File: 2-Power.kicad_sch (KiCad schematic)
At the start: 17 parts, among them J201 DC IN 5.5/2.1mm, J202 9V battery clip, U201 ZXMP3A17E6TA

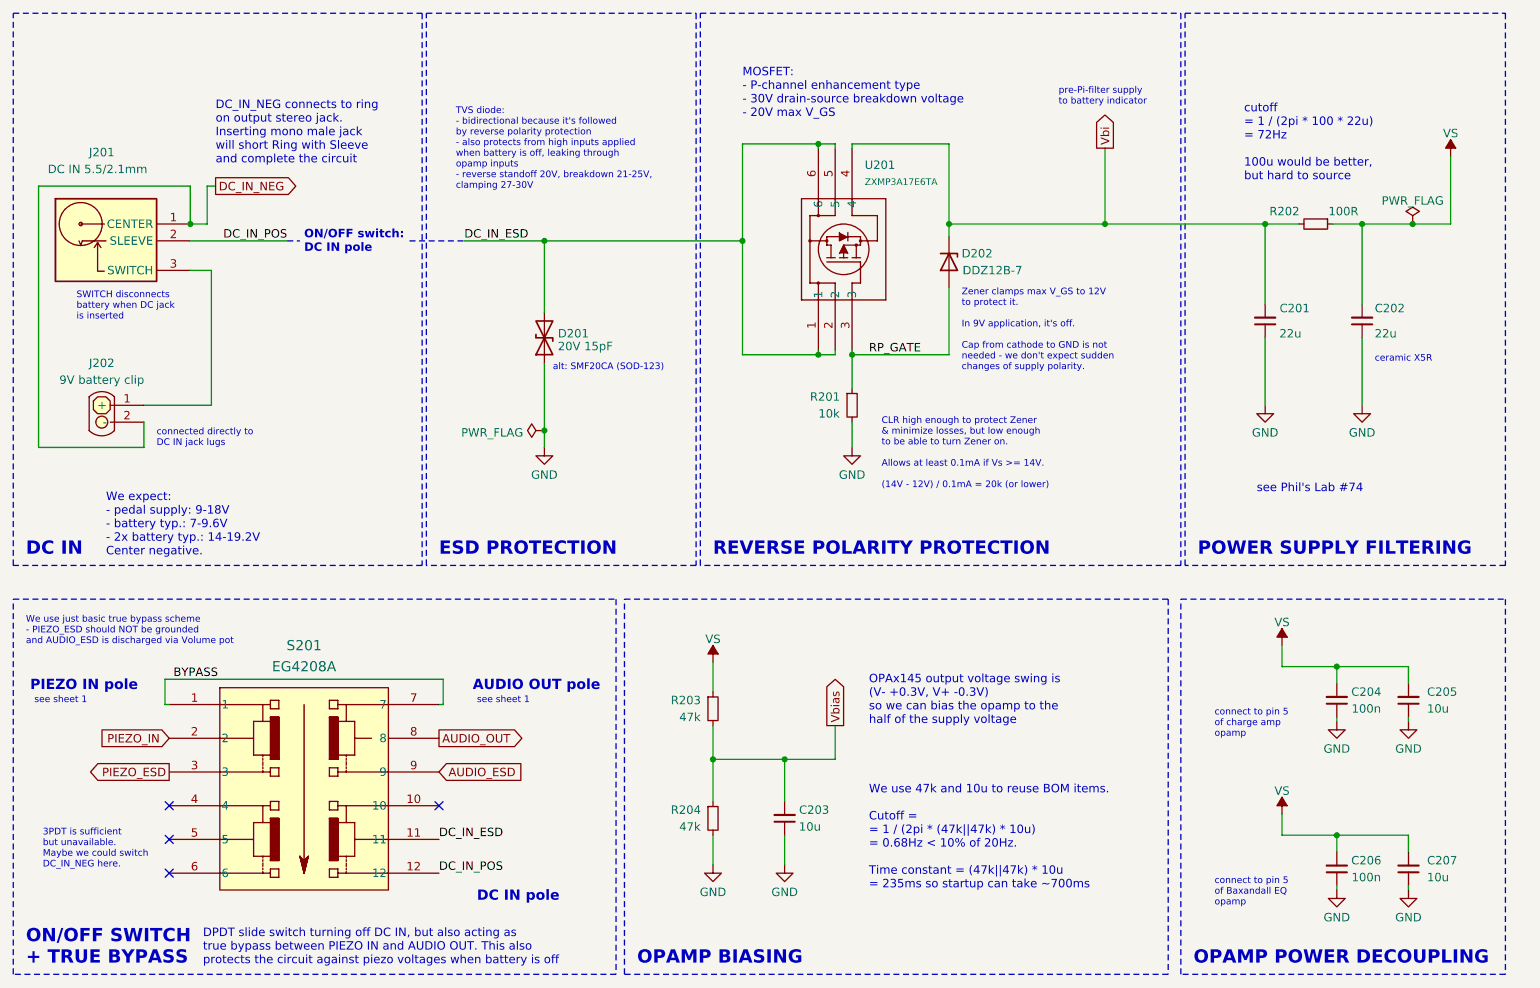
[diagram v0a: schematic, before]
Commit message: aligning schematics to grid, swapping switches as they are on the bottom side now; rough placement of BI section on board
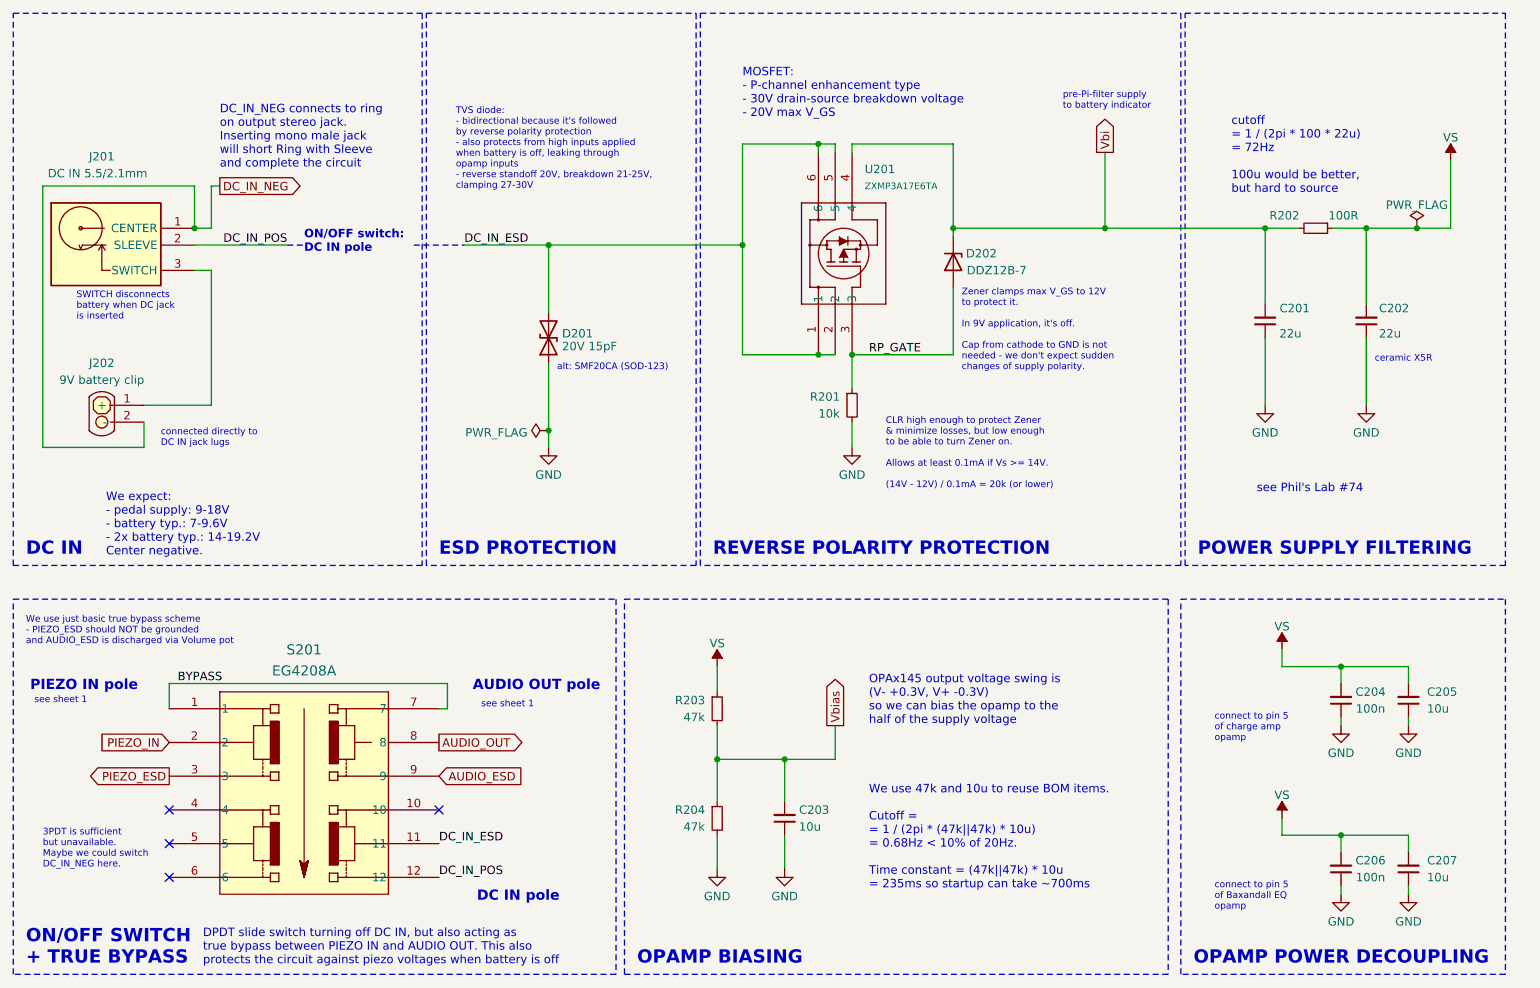
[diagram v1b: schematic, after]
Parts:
- J201: footprint library:694106301002 -> 694106301002_1; Manufacturer_Name (none) -> Wurth Elektronik; Manufacturer_Part_Number (none) -> 694106301002; Mouser Part Number (none) -> 710-694106301002; Mouser Price/Stock (none) -> https://www.mouser.co.uk/ProductDetail/Wurth-Elektronik/694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
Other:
- moved on the sheet: C202, C204, C206, D201, D202, J201, R202, R203, R204, S201, U201

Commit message: schematics: replacing the switches, rewiring, improving center switch positions, removing 6n8 cap
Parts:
- removed J202: 9V battery clip, symbol 9VBatteryConn:9VBatteryConn
- J201: footprint 694106301002_1 -> library:694106301002; Manufacturer_Name Wurth Elektronik -> (none); Manufacturer_Part_Number 694106301002 -> (none); Mouser Part Number 710-694106301002 -> (none); Mouser Price/Stock https://www.mouser.co.uk/ProductDetail/Wurth-Elektronik/694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 -> (none)
- S201: Source (none) -> Mouser
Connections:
- net DC_IN_ESD: now also S201.5; no longer S201.11
- net DC_IN_POS: now also S201.6; no longer S201.12
- net DC_IN_SW: now reaches J201.3 (SWITCH)
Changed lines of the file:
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@@
 	)
 	(no_connect
-		(at 49.53 142.24)
+		(at 90.17 142.24)
 	)
 	(no_connect
@@
 	)
 	(no_connect
-		(at 49.53 147.32)
+		(at 90.17 147.32)
 	)
 	(wire
@@
 	(text "3PDT is sufficient\nbut unavailable.\nMaybe we could switch\nDC_IN_NEG here."
 		(exclude_from_sim no)
-		(at 30.48 146.05 0)
+		(at 100.33 151.13 0)
 		(effects
 			(font
@@
 	(text "DC IN pole"
 		(exclude_from_sim no)
-		(at 95.885 151.13 0)
+		(at 30.48 151.13 0)
 		(effects
 			(font
@@
 	)
 	(label "DC_IN_ESD"
-		(at 90.17 142.24 0)
+		(at 49.53 142.24 180)
 		(fields_autoplaced yes)
 		(effects
@@
 				(size 1.27 1.27)
 			)
-			(justify left bottom)
+			(justify right bottom)
 		)
 	)
@@
 	)
 	(label "DC_IN_POS"
-		(at 90.17 147.32 0)
+		(at 49.53 147.32 180)
 		(fields_autoplaced yes)
 		(effects
@@
 				(size 1.27 1.27)
 			)
-			(justify left bottom)
+			(justify right bottom)
 		)
 	)
@@
 		)
 	)
+	(label "DC_IN_SW"
+		(at 55.88 67.31 0)
+		(fields_autoplaced yes)
+		(effects
+			(font
+				(size 1.27 1.27)
+			)
+			(justify left bottom)
+		)
+	)
 	(global_label "DC_IN_NEG"
 		(shape output)
@@
 			)
 		)
-		(property "Description" ""
+		(property "Description" "Power symbol creates a global label with name \"VS\""
 			(at 242.57 39.37 0)
 			(effects
@@
 			)
 		)
+		(property "Purpose" ""
+			(at 242.57 39.37 0)
+			(effects
+				(font
+					(size 1.27 1.27)
+				)
+			)
+		)
 		(pin "1"
 		)
@@
 			)
 		)
-		(property "Description" ""
+		(property "Description" "Power symbol creates a global label with name \"GND\" , ground"
 			(at 226.06 149.86 0)
 			(effects
@@
 			)
 		)
-		(property "Description" ""
+		(property "Description" "Special symbol for telling ERC where power comes from"
 			(at 106.68 80.01 0)
 			(effects
@@
 			)
 		)
+		(property "Purpose" ""
+			(at 106.68 80.01 0)
+			(effects
+				(font
+					(size 1.27 1.27)
+				)
+			)
+		)
 		(pin "1"
 		)
@@
 	)
 	(symbol
+		(lib_name "PWR_FLAG_1")
 		(lib_id "power:PWR_FLAG")
 		(at 237.49 49.53 0)
@@
 			)
 		)
-		(property "Description" ""
+		(property "Description" "Special symbol for telling ERC where power comes from"
 			(at 237.49 49.53 0)
 			(effects
@@
 			)
 		)
+		(property "Purpose" ""
+			(at 237.49 49.53 0)
+			(effects
+				(font
+					(size 1.27 1.27)
+				)
+			)
+		)
 		(pin "1"
 		)
@@
 			)
 		)
-		(property "Source" ""
+		(property "Source" "Mouser"
 			(at 49.53 121.92 0)
 			(effects
@@
 			)
 		)
-		(property "Description" ""
+		(property "Description" "Power symbol creates a global label with name \"GND\" , ground"
 			(at 226.06 124.46 0)
 			(effects
@@
 			)
 		)
-		(property "Description" ""
+		(property "Description" "Power symbol creates a global label with name \"GND\" , ground"
 			(at 132.08 146.05 0)
 			(effects
@@
 			)
 		)
-		(property "Description" ""
+		(property "Description" "Power symbol creates a global label with name \"GND\" , ground"
 			(at 236.22 149.86 0)
 			(effects
@@
 	)
 	(symbol
+		(lib_name "VS_1")
 		(lib_id "power:VS")
 		(at 132.08 115.57 0)
@@
 			)
 		)
-		(property "Description" ""
+		(property "Description" "Power symbol creates a global label with name \"VS\""
 			(at 132.08 115.57 0)
 			(effects
@@
 			)
 		)
+		(property "Purpose" ""
+			(at 132.08 115.57 0)
+			(effects
+				(font
+					(size 1.27 1.27)
+				)
+			)
+		)
 		(pin "1"
 		)
@@
 	)
 	(symbol
+		(lib_name "VS_3")
 		(lib_id "power:VS")
 		(at 217.17 138.43 0)
@@
 			)
 		)
-		(property "Description" ""
+		(property "Description" "Power symbol creates a global label with name \"VS\""
 			(at 217.17 138.43 0)
 			(effects
@@
 			)
 		)
-		(property "Description" ""
+		(property "Description" "Power symbol creates a global label with name \"GND\" , ground"
 			(at 142.24 146.05 0)
 			(effects
@@
 			)
 		)
-		(property "Footprint" "694106301002_1"
+		(property "Footprint" "library:694106301002"
 			(at 67.31 146.99 0)
 			(effects
@@
 			)
 		)
-		(property "Manufacturer_Name" "Wurth Elektronik"
-			(at 67.31 546.99 0)
-			(effects
-				(font
-					(size 1.27 1.27)
-				)
-				(justify left top)
-				(hide yes)
-			)
-		)
-		(property "Manufacturer_Part_Number" "694106301002"
-			(at 67.31 646.99 0)
-			(effects
-				(font
-					(size 1.27 1.27)
-				)
-				(justify left top)
-				(hide yes)
-			)
-		)
-		(property "Mouser Part Number" "710-694106301002"
-			(at 67.31 746.99 0)
-			(effects
-				(font
-					(size 1.27 1.27)
-				)
-				(justify left top)
-				(hide yes)
-			)
-		)
-		(property "Mouser Price/Stock" "https://www.mouser.co.uk/ProductDetail/Wurth-Elektronik/694106301002?qs=a9WhcLg8qCwOEkcI62k5mA%3D%3D"
-			(at 67.31 846.99 0)
-			(effects
-				(font
-					(size 1.27 1.27)
-				)
-				(justify left top)
-				(hide yes)
-			)
-		)
-		(property "Arrow Part Number" ""
-			(at 67.31 946.99 0)
-			(effects
-				(font
-					(size 1.27 1.27)
-				)
-				(justify left top)
-				(hide yes)
-			)
-		)
-		(property "Arrow Price/Stock" ""
-			(at 67.31 1046.99 0)
-			(effects
-				(font
-					(size 1.27 1.27)
-				)
-				(justify left top)
-				(hide yes)
-			)
-		)
 		(pin "3"
 		)
@@
 			)
 		)
-		(property "Description" ""
+		(property "Description" "Power symbol creates a global label with name \"GND\" , ground"
 			(at 106.68 82.55 0)
 			(effects
@@
 	)
 	(symbol
-		(lib_id "9VBatteryConn:9VBatteryConn")
-		(at 39.37 77.47 0)
-		(unit 1)
-		(exclude_from_sim no)
-		(in_bom yes)
-		(on_board no)
-		(dnp no)
-		(property "Reference" "J202"
-			(at 39.37 69.85 0)
-			(effects
-				(font
-					(size 1.27 1.27)
-				)
-			)
-		)
-		(property "Value" "9V battery clip"
-			(at 39.37 72.39 0)
-			(effects
-				(font
-					(size 1.27 1.27)
-				)
-			)
-		)
-		(property "Footprint" ""
-			(at 39.37 74.295 0)
-			(effects
-				(font
-					(size 1.27 1.27)
-				)
-				(hide yes)
-			)
-		)
-		(property "Datasheet" "https://www.tme.eu/Document/28400c41ff141df9883113179bef4075/BS.pdf"
-			(at 39.37 74.295 0)
-			(effects
-				(font
-					(size 1.27 1.27)
-				)
-				(hide yes)
-			)
-		)
-		(property "Description" ""
-			(at 39.37 77.47 0)
-			(effects
-				(font
-					(size 1.27 1.27)
-				)
-				(hide yes)
-			)
-		)
-		(property "Purpose" "internal 9V battery connector"
-			(at 39.37 77.47 0)
-			(effects
-				(font
-					(size 1.27 1.27)
-				)
-				(hide yes)
-			)
-		)
-		(property "Mfr" "COMF"
-			(at 39.37 77.47 0)
-			(effects
-				(font
-					(size 1.27 1.27)
-				)
-				(hide yes)
-			)
-		)
-		(property "Mfr Part #" "BS-IC"
-			(at 39.37 77.47 0)
-			(effects
-				(font
-					(size 1.27 1.27)
-				)
-				(hide yes)
-			)
-		)
-		(property "Mouser Part #" "-"
-			(at 39.37 77.47 0)
-			(effects
-				(font
-					(size 1.27 1.27)
-				)
-				(hide yes)
-			)
-		)
-		(property "LCSC Part #" "-"
-			(at 39.37 77.47 0)
-			(effects
-				(font
-					(size 1.27 1.27)
-				)
-				(hide yes)
-			)
-		)
-		(property "TME Part #" "BS-IC"
-			(at 39.37 77.47 0)
-			(effects
-				(font
-					(size 1.27 1.27)
-				)
-				(hide yes)
-			)
-		)
-		(property "Source" "TME"
-			(at 39.37 77.47 0)
-			(effects
-				(font
-					(size 1.27 1.27)
-				)
-				(hide yes)
-			)
-		)
-		(pin "2"
-		)
-		(pin "1"
-		)
-		(instances
-			(project "2023_PiezoPreamp"
-				(path "/6e141482-2809-49ad-b316-4cdedc98ad26/b10e95cd-10a1-4d25-b6a0-2bd4304f390c"
-					(reference "J202")
-					(unit 1)
-				)
-			)
-		)
-	)
-	(symbol
 		(lib_id "Device:C_Small")
 		(at 236.22 120.65 180)
@@
 	)
 	(symbol
+		(lib_name "VS_2")
 		(lib_id "power:VS")
 		(at 217.17 113.03 0)
@@
 			)
 		)
-		(property "Description" ""
+		(property "Description" "Power symbol creates a global label with name \"VS\""
 			(at 217.17 113.03 0)
 			(effects
@@
 			)
 		)
-		(property "Description" ""
+		(property "Description" "Power symbol creates a global label with name \"GND\" , ground"
 			(at 236.22 124.46 0)
 			(effects
@@
 			)
 		)
-		(property "Description" ""
+		(property "Description" "Power symbol creates a global label with name \"GND\" , ground"
 			(at 152.4 82.55 0)
 			(effects
@@
 			)
 		)
-		(property "Description" ""
+		(property "Description" "Power symbol creates a global label with name \"GND\" , ground"
 			(at 229.87 76.2 0)
 			(effects
@@
 			)
 		)
-		(property "Description" ""
+		(property "Description" "Power symbol creates a global label with name \"GND\" , ground"
 			(at 214.63 76.2 0)
 			(effects

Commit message: schematic: renaming low-pass filter to high-pass filter as it was named incorrectly lol
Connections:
- net DC_IN_ESD: now also S201.11; no longer S201.5
- net DC_IN_POS: now also S201.12; no longer S201.6
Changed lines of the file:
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@@
 	)
 	(no_connect
-		(at 90.17 142.24)
+		(at 49.53 142.24)
 	)
 	(no_connect
@@
 	)
 	(no_connect
-		(at 90.17 147.32)
+		(at 49.53 147.32)
 	)
 	(wire
@@
 	(text "3PDT is sufficient\nbut unavailable.\nMaybe we could switch\nDC_IN_NEG here."
 		(exclude_from_sim no)
-		(at 100.33 151.13 0)
+		(at 29.21 147.32 0)
 		(effects
 			(font
@@
 	(text "DC IN pole"
 		(exclude_from_sim no)
-		(at 30.48 151.13 0)
+		(at 99.06 151.13 0)
 		(effects
 			(font
@@
 	)
 	(label "DC_IN_ESD"
-		(at 49.53 142.24 180)
+		(at 90.17 142.24 0)
 		(fields_autoplaced yes)
 		(effects
@@
 				(size 1.27 1.27)
 			)
-			(justify right bottom)
+			(justify left bottom)
 		)
 	)
@@
 	)
 	(label "DC_IN_POS"
-		(at 49.53 147.32 180)
+		(at 90.17 147.32 0)
 		(fields_autoplaced yes)
 		(effects
@@
 				(size 1.27 1.27)
 			)
-			(justify right bottom)
-		)
-	)
+			(justify left bottom)
+		)
+	)

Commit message: fixing missing DC jack; continued working on the board layout
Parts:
- added J202: 9V Battery Connector, symbol 9VBatteryConn:9VBatteryConn
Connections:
- net DC_IN_NEG: now also J202.2 (-)
- net DC_IN_SW: now also J202.1 (+)
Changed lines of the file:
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@@
+	)
+	(symbol
+		(lib_id "9VBatteryConn:9VBatteryConn")
+		(at 39.37 77.47 0)
+		(unit 1)
+		(exclude_from_sim no)
+		(in_bom yes)
+		(on_board yes)
+		(dnp no)
+		(property "Reference" "J202"
+			(at 33.02 69.85 0)
+			(effects
+				(font
+					(size 1.27 1.27)
+				)
+				(justify left)
+			)
+		)
+		(property "Value" "9V Battery Connector"
+			(at 33.02 72.39 0)
+			(effects
+				(font
+					(size 1.27 1.27)
+				)
+				(justify left)
+			)
+		)
+		(property "Footprint" ""
+			(at 39.37 74.295 0)
+			(effects
+				(font
+					(size 1.27 1.27)
+				)
+				(hide yes)
+			)
+		)
+		(property "Datasheet" ""
+			(at 39.37 74.295 0)
+			(effects
+				(font
+					(size 1.27 1.27)
+				)
+				(hide yes)
+			)
+		)
+		(property "Description" ""
+			(at 39.37 77.47 0)
+			(effects
+				(font
+					(size 1.27 1.27)
+				)
+				(hide yes)
+			)
+		)
+		(property "Purpose" ""
+			(at 39.37 77.47 0)
+			(effects
+				(font
+					(size 1.27 1.27)
+				)
+			)
+		)
+		(pin "1"
+		)
+		(pin "2"
+		)
+		(instances
+			(project "2023_PiezoPreamp"
+				(path "/6e141482-2809-49ad-b316-4cdedc98ad26/b10e95cd-10a1-4d25-b6a0-2bd4304f390c"
+					(reference "J202")
+					(unit 1)
+				)
+			)
+		)
 	)
 	(symbol
